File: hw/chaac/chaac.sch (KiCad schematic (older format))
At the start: 85 parts, among them J1 windrain, J10 Therm, J11 FAN, J2 Conn_01x02, J3 UART, J4 Battery, J5 Power, J6 Light, J7 AM2315, J8 TC2030-CTX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

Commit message: Began placement for chaac
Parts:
- removed L2: 47nH, Inductor_SMD:L_0603_1608Metric, symbol Device:L_Small
- removed R13, R14: 0, Resistor_SMD:R_0603_1608Metric, symbol Device:R_Small
- added C31: 0.1uF, Capacitor_SMD:C_0603_1608Metric, symbol Device:C_Small
- C11: value 22pF -> 0.1uF; DKPN 1276-2228-1-ND -> 490-1532-1-ND; MPN CL10C220JB8NFNC -> GRM188R71C104KA01D
- U7: footprint (none) -> alvarop:XCL102
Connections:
- net GPS_RXD is gone; now on net BATT: C11.1
- net GND: now also C31.2
- net LIGHT: now also C31.1
- net UART_TX: now also J3.3 (Pin_3)
- no-connect marks 24 -> 25
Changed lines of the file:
@@
 Text Label 2650 10900 1    50   ~ 0
 GPS_TXD
-Text Label 2750 10900 1    50   ~ 0
-GPS_RXD
 $Comp
 L power:+3.3V #PWR05
@@
 	8050 10450 8350 10450
 Wire Wire Line
-	8350 10450 8350 10550
+	8350 10450 8350 10650
 Wire Wire Line
 	8050 10550 8200 10550
@@
 L power:GND #PWR010
 U 1 1 5BAABEB2
-P 8350 10550
-F 0 "#PWR010" H 8350 10300 50  0001 C CNN
-F 1 "GND" H 8355 10377 50  0000 C CNN
-F 2 "" H 8350 10550 50  0001 C CNN
-F 3 "" H 8350 10550 50  0001 C CNN
-	1    8350 10550
-	1    0    0    -1
-$EndComp
-Wire Wire Line
-	8050 10350 8350 10350
-Text Label 8350 10350 2    50   ~ 0
+P 8350 10750
+F 0 "#PWR010" H 8350 10500 50  0001 C CNN
+F 1 "GND" H 8355 10577 50  0000 C CNN
+F 2 "" H 8350 10750 50  0001 C CNN
+F 3 "" H 8350 10750 50  0001 C CNN
+	1    8350 10750
+	1    0    0    -1
+$EndComp
+Wire Wire Line
+	8050 10350 8500 10350
+Text Label 8750 10350 2    50   ~ 0
 LIGHT
 $Comp
@@
 Text Label 8800 3000 2    50   ~ 0
 XB_TX
-Wire Wire Line
-	2200 1900 1850 1900
-Text Label 1850 1900 0    50   ~ 0
-GPS_RXD
 Wire Wire Line
 	8400 3300 8800 3300
@@
 	2000 10200 2150 10200
 $Comp
-L Device:L_Small L2
-U 1 1 5C41F42C
-P 2750 10300
-F 0 "L2" H 2798 10346 50  0000 L CNN
-F 1 "47nH" H 2798 10255 50  0000 L CNN
-F 2 "Inductor_SMD:L_0603_1608Metric" H 2750 10300 50  0001 C CNN
-F 3 "~" H 2750 10300 50  0001 C CNN
-F 4 " ‎L-14C47NJV4T" H 2750 10300 50  0001 C CNN "MPN"
-F 5 "712-1442-1-ND‎" H 2750 10300 50  0001 C CNN "DKPN"
-	1    2750 10300
-	1    0    0    -1
-$EndComp
-$Comp
 L Device:L_Small L1
 U 1 1 5C41F6C3
@@
 Wire Wire Line
 	2650 10200 2650 10150
-Wire Wire Line
-	2750 10150 2750 10200
 $Comp
 L power:GND #PWR0110
@@
 Wire Wire Line
 	2650 10400 2650 10500
-Wire Wire Line
-	2750 10400 2750 10500
 $Comp
 L Device:C_Small C8
@@
 	0    -1   -1   0
 $EndComp
-$Comp
-L Device:C_Small C11
-U 1 1 5C49A200
-P 2950 10500
-F 0 "C11" H 2750 10550 50  0000 L CNN
-F 1 "22pF" H 2700 10450 50  0000 L CNN
-F 2 "Capacitor_SMD:C_0603_1608Metric" H 2950 10500 50  0001 C CNN
-F 3 "~" H 2950 10500 50  0001 C CNN
-F 4 "1276-2228-1-ND" H 0   0   50  0001 C CNN "DKPN"
-F 5 "CL10C220JB8NFNC" H 0   0   50  0001 C CNN "MPN"
-	1    2950 10500
-	0    -1   -1   0
-$EndComp
-Wire Wire Line
-	2850 10500 2750 10500
-Connection ~ 2750 10500
-Wire Wire Line
-	2750 10500 2750 10900
 Wire Wire Line
 	2650 10500 2550 10500
@@
 Wire Wire Line
 	2300 10500 2350 10500
-$Comp
-L power:GND #PWR0115
-U 1 1 5C4BAD54
-P 3100 10500
-F 0 "#PWR0115" H 3100 10250 50  0001 C CNN
-F 1 "GND" H 3105 10327 50  0000 C CNN
-F 2 "" H 3100 10500 50  0001 C CNN
-F 3 "" H 3100 10500 50  0001 C CNN
-	1    3100 10500
-	0    -1   -1   0
-$EndComp
-Wire Wire Line
-	3050 10500 3100 10500
 Wire Wire Line
 	2050 9650 1650 9650
@@
 UART_RX
 $Comp
-L Device:R_Small R13
-U 1 1 5C9B2177
-P 2300 1750
-F 0 "R13" V 2350 1650 50  0000 C CNN
-F 1 "0" V 2300 1750 50  0000 C CNN
-F 2 "Resistor_SMD:R_0603_1608Metric" H 2300 1750 50  0001 C CNN
-F 3 "~" H 2300 1750 50  0001 C CNN
-	1    2300 1750
-	0    -1   -1   0
-$EndComp
-$Comp
-L Device:R_Small R14
-U 1 1 5C9C0DF4
-P 2300 1900
-F 0 "R14" V 2250 2000 50  0000 C CNN
-F 1 "0" V 2300 1900 50  0000 C CNN
-F 2 "Resistor_SMD:R_0603_1608Metric" H 2300 1900 50  0001 C CNN
-F 3 "~" H 2300 1900 50  0001 C CNN
-	1    2300 1900
-	0    1    1    0
-$EndComp
-Wire Wire Line
-	2400 1750 2450 1750
-Wire Wire Line
-	2050 1750 2200 1750
-Wire Wire Line
-	2400 1900 2450 1900
-Wire Wire Line
-	2450 1900 2450 1750
-Connection ~ 2450 1750
-Wire Wire Line
-	2450 1750 2800 1750
-$Comp
 L Device:R_Small R7
 U 1 1 5CAA119E
@@
 $EndComp
 Wire Wire Line
-	1000 1350 1000 1500
+	1000 1350 1000 1450
 Wire Wire Line
 	1000 850  1000 700
@@
 Wire Wire Line
 	1000 1100 1000 1150
-Text Label 1350 1100 2    50   ~ 0
+Text Label 1550 1100 2    50   ~ 0
 BATT
 $Comp
@@
 U 1 1 5CE242B1
 P 14350 7600
-F 0 "R22" V 14450 7750 50  0000 R CNN
+F 0 "R22" V 14550 7750 50  0000 R CNN
 F 1 "10k" V 14450 7650 50  0000 R CNN
 F 2 "Resistor_SMD:R_0603_1608Metric" H 14350 7600 50  0001 C CNN
@@
 U 1 1 5CE248E2
 P 14350 7900
-F 0 "R23" V 14450 8050 50  0000 R CNN
+F 0 "R23" V 14550 8050 50  0000 R CNN
 F 1 "10k" V 14450 7950 50  0000 R CNN
 F 2 "Resistor_SMD:R_0603_1608Metric" H 14350 7900 50  0001 C CNN
@@
 U 1 1 5CE2498A
 P 14350 8250
-F 0 "R24" V 14250 8350 50  0000 R CNN
+F 0 "R24" V 14200 8350 50  0000 R CNN
 F 1 "10k" V 14250 8200 50  0000 R CNN
 F 2 "Resistor_SMD:R_0603_1608Metric" H 14350 8250 50  0001 C CNN
@@
 P 11400 7800
 F 0 "R17" V 11500 7950 50  0000 R CNN
-F 1 "10k" V 11500 7850 50  0000 R CNN
+F 1 "10k" V 11500 7750 50  0000 R CNN
 F 2 "Resistor_SMD:R_0603_1608Metric" H 11400 7800 50  0001 C CNN
 F 3 "~" H 11400 7800 50  0001 C CNN
@@
 F 0 "U7" H 2250 4800 60  0000 C CNN
 F 1 "XCL102" H 2250 4694 60  0000 C CNN
-F 2 "" H 1800 4200 50  0001 C CNN
+F 2 "alvarop:XCL102" H 1800 4200 50  0001 C CNN
 F 3 "" H 1800 4200 50  0001 C CNN
 	1    2250 4100
@@
 Wire Wire Line
 	3500 4300 3550 4300
+Wire Wire Line
+	2050 1750 2800 1750
+NoConn ~ 2750 10150
+$Comp
+L Device:C_Small C11
+U 1 1 5DEB196A
+P 1350 1300
+F 0 "C11" H 1200 1450 50  0000 L CNN
+F 1 "0.1uF" H 1100 1200 50  0000 L CNN
+F 2 "Capacitor_SMD:C_0603_1608Metric" H 1350 1300 50  0001 C CNN
+F 3 "~" H 1350 1300 50  0001 C CNN
+F 4 "490-1532-1-ND" H -4900 -7050 50  0001 C CNN "DKPN"
+F 5 "GRM188R71C104KA01D" H -4900 -7050 50  0001 C CNN "MPN"
+	1    1350 1300
+	1    0    0    -1
+$EndComp
+Wire Wire Line
+	1350 1200 1350 1100
+Connection ~ 1350 1100
+Wire Wire Line
+	1350 1100 1550 1100
+Wire Wire Line
+	1350 1400 1350 1450
+Wire Wire Line
+	1350 1450 1000 1450
+Connection ~ 1000 1450
+Wire Wire Line
+	1000 1450 1000 1500
+$Comp
+L Device:C_Small C31
+U 1 1 5DF1B210
+P 8500 10500
+F 0 "C31" H 8600 10450 50  0000 L CNN
+F 1 "0.1uF" H 8550 10600 50  0000 L CNN
+F 2 "Capacitor_SMD:C_0603_1608Metric" H 8500 10500 50  0001 C CNN
+F 3 "~" H 8500 10500 50  0001 C CNN
+F 4 "490-1532-1-ND" H 2250 2150 50  0001 C CNN "DKPN"
+F 5 "GRM188R71C104KA01D" H 2250 2150 50  0001 C CNN "MPN"
+	1    8500 10500
+	1    0    0    -1
+$EndComp
+Wire Wire Line
+	8500 10400 8500 10350
+Connection ~ 8500 10350
+Wire Wire Line
+	8500 10350 8750 10350
+Wire Wire Line
+	8500 10600 8500 10650
+Wire Wire Line
+	8500 10650 8350 10650
+Connection ~ 8350 10650
+Wire Wire Line
+	8350 10650 8350 10750
 $EndSCHEMATC

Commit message: Removed GPS, re-did placement
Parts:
- removed ANT1: SR4G008, alvarop:SR4G008, symbol alvarop:SR4G008
- removed C13, C15, C6, C8: 22pF, Capacitor_SMD:C_0603_1608Metric, symbol Device:C_Small
- removed C7: 2.2uF, Capacitor_SMD:C_0603_1608Metric, symbol Device:C_Small
- removed C9: 1.5pF, Capacitor_SMD:C_0402_1005Metric, symbol Device:C_Small
- removed L1: 47nH, Inductor_SMD:L_0603_1608Metric, symbol Device:L_Small
- removed L3: 12nH, Inductor_SMD:L_0402_1005Metric, symbol Device:L_Small
- removed L4: DNP, Inductor_SMD:L_0402_1005Metric, symbol Device:L_Small
- removed U4: M10578-A2, alvarop:M10578-A2, symbol alvarop:M10578-A2
- added J12: AM2315, Connector_PinHeader_2.54mm:PinHeader_1x04_P2.54mm_Vertical, symbol Connector_Generic:Conn_01x04
- added R13: 0, Resistor_SMD:R_0603_1608Metric, symbol Device:R_Small
- R11: value 10k -> 0; DKPN 311-10.0KHRCT-ND -> (none); MPN RC0603FR-0710KL -> (none)
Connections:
- net +3V3: now also J12.2 (Pin_2)
- net GND: now also J12.1 (Pin_1); no longer R11.1
- net GPS_SBY: now also U2.31 (PH3/BOOT0), J12.4 (Pin_4); no longer U2.26 (PB3)
- net LED1: now also U2.21 (PA11); no longer U2.27 (PB4)
- net UART_RX: now also R11.1, R13.1; no longer J3.2 (Pin_2)
- net GPS_TX: now reaches R11.2
- net GPS_TX: now also J12.3 (Pin_3)
- net GPS_FIX: no longer names the net of U2.15 (PB1)
- net GPS_TXD: no longer names the net of U2.25 (PA15/SWO)
- new net: J3.2 (Pin_2), R13.2
- no-connect marks 25 -> 21
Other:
- moved on the sheet: C10, C12, C14, J1, R1, R15, R2, R3, R4, R5, R6

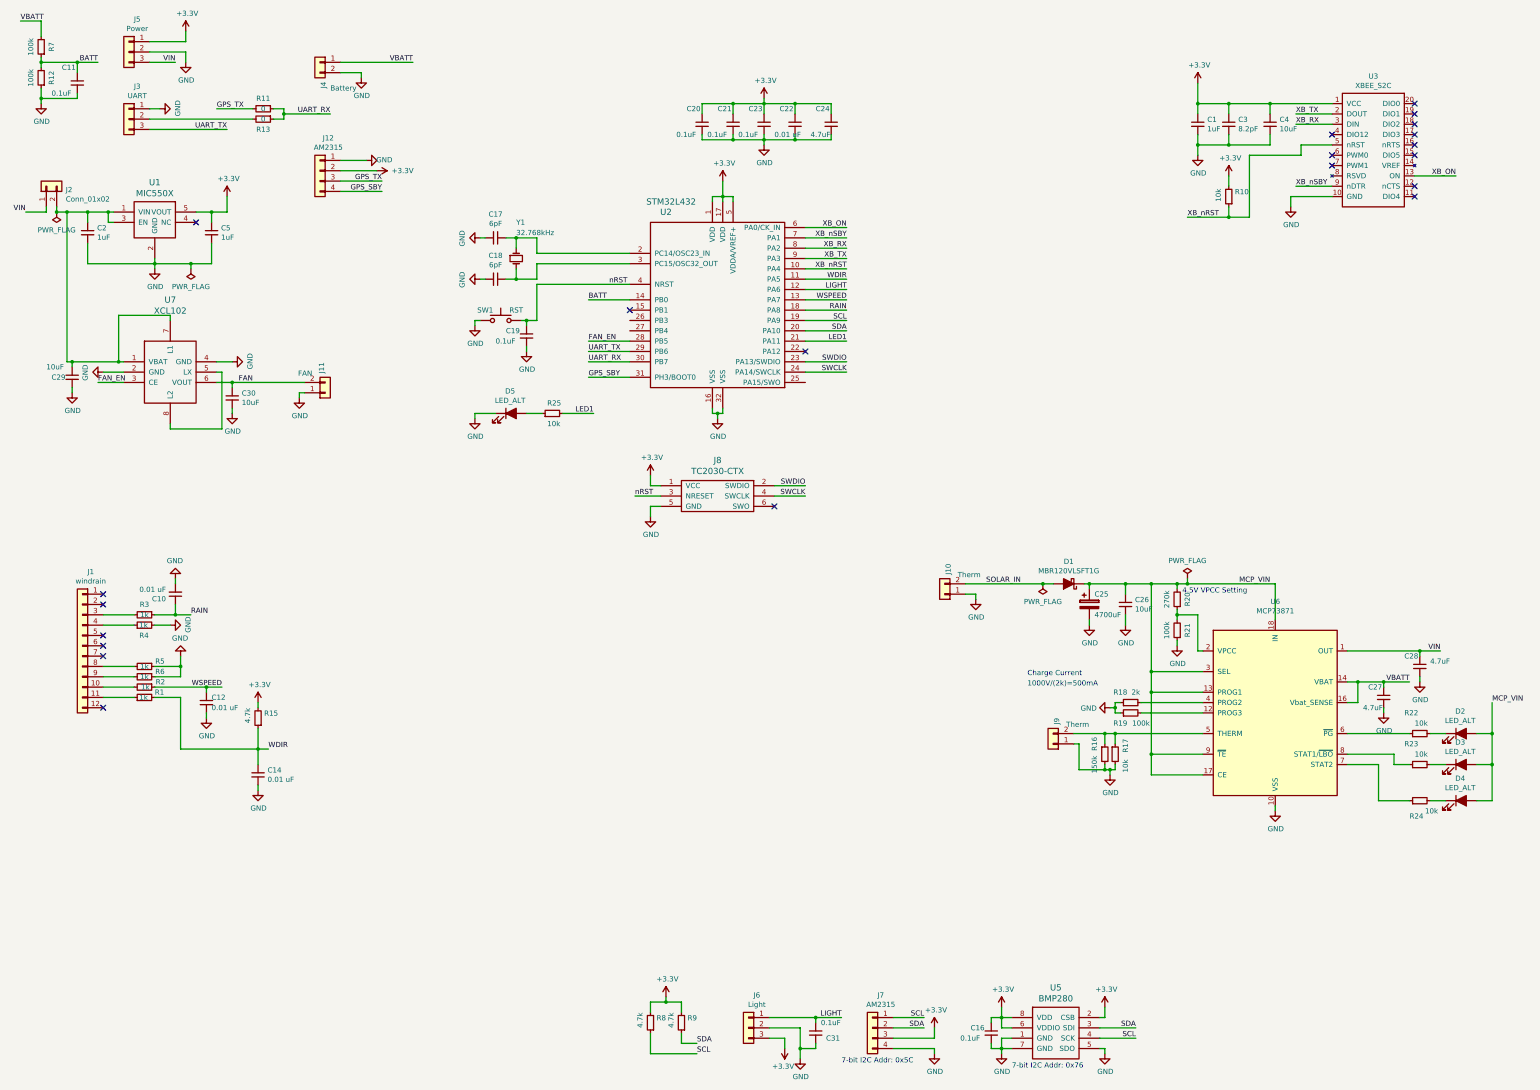
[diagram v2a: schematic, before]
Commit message: Finished chaac 1.0 schematic and layout
Released to JLCPCB
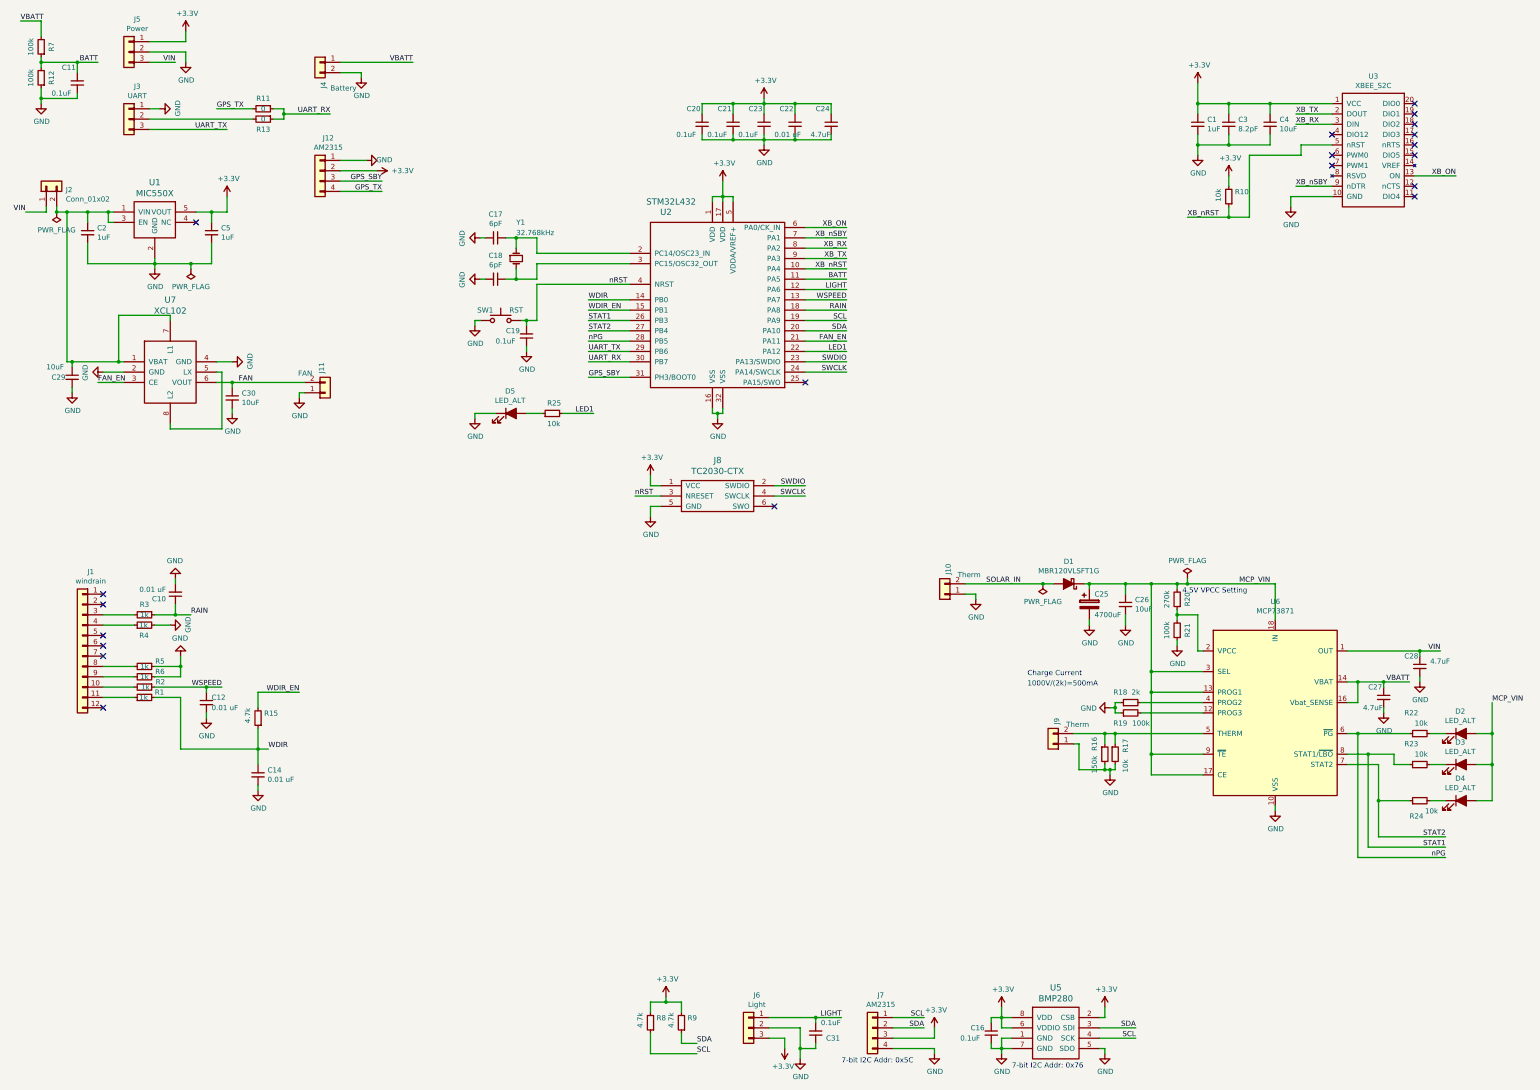
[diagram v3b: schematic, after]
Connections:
- net +3V3: no longer R15.2
- net BATT: now also U2.11 (PA5); no longer U2.14 (PB0)
- net FAN_EN: now also U2.21 (PA11); no longer U2.28 (PB5)
- net GPS_SBY: now also J12.3 (Pin_3); no longer J12.4 (Pin_4)
- net GPS_TX: now also J12.4 (Pin_4); no longer J12.3 (Pin_3)
- net LED1: now also U2.22 (PA12); no longer U2.21 (PA11)
- net WDIR: now also U2.14 (PB0); no longer U2.11 (PA5)
- net WDIR_EN: now reaches U2.15 (PB1)
- net WDIR_EN: now also R15.2
- net STAT1: now reaches U2.26 (PB3)
- net STAT1: now also R23.1, U6.8 (STAT1/~LBO~)
- net STAT2: now reaches U2.27 (PB4)
- net STAT2: now also R24.1, U6.7 (STAT2)
- net nPG: now reaches R22.1, U6.6 (~PG~)
- net nPG: now also U2.28 (PB5)
- no-connect marks 21 -> 20
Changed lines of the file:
@@
 Sheet 1 1
 Title "Chaac"
-Date "2019-01-02"
+Date "2019-01-03"
 Rev "1.0"
 Comp "@alvaroprieto"
@@
 Wire Wire Line
 	8400 3200 8800 3200
-Text Label 8800 3200 2    50   ~ 0
+Text Label 6300 3400 0    50   ~ 0
 WDIR
 Wire Wire Line
@@
 Wire Wire Line
 	3100 7550 3100 7750
-$Comp
-L power:+3.3V #PWR0123
-U 1 1 5C2B14C9
-P 3100 7300
-F 0 "#PWR0123" H 3100 7150 50  0001 C CNN
-F 1 "+3.3V" H 3115 7473 50  0000 C CNN
-F 2 "" H 3100 7300 50  0001 C CNN
-F 3 "" H 3100 7300 50  0001 C CNN
-	1    3100 7300
-	1    0    0    -1
-$EndComp
-Wire Wire Line
-	3100 7300 3100 7350
 Text Label 3200 7750 0    50   ~ 0
 WDIR
@@
 Text Label 6300 4000 0    50   ~ 0
 UART_RX
-Text Label 6300 3400 0    50   ~ 0
+Text Label 8800 3200 2    50   ~ 0
 BATT
 Wire Wire Line
@@
 $EndComp
 Wire Wire Line
-	14250 7600 13650 7600
-Wire Wire Line
-	13650 7800 14100 7800
+	14250 7600 13750 7600
+Wire Wire Line
+	13650 7800 13850 7800
 Wire Wire Line
 	14100 7800 14100 7900
@@
 	1    0    0    -1
 $EndComp
-NoConn ~ 8400 3900
 $Comp
 L power:PWR_FLAG #FLG0106
@@
 Wire Wire Line
 	12100 6150 12950 6150
-Text Label 8800 3800 2    50   ~ 0
+Text Label 8800 3900 2    50   ~ 0
 LED1
 $Comp
@@
 	5200 4500 5200 4550
 Wire Wire Line
-	6700 3800 6300 3800
-Text Label 6300 3800 0    50   ~ 0
+	8400 3800 8800 3800
+Text Label 8800 3800 2    50   ~ 0
 FAN_EN
 $Comp
@@
 	0    1    1    0
 $EndComp
+Text Label 4300 2250 2    50   ~ 0
+GPS_SBY
 Text Label 4300 2350 2    50   ~ 0
-GPS_SBY
-Text Label 4300 2250 2    50   ~ 0
 GPS_TX
 Wire Wire Line
-	8400 3800 8800 3800
-NoConn ~ 6700 3500
+	8400 3900 8800 3900
+Wire Wire Line
+	6700 3500 6300 3500
+Text Label 6300 3500 0    50   ~ 0
+WDIR_EN
+Text Label 3500 7200 2    50   ~ 0
+WDIR_EN
+Wire Wire Line
+	3100 7200 3500 7200
+Wire Wire Line
+	3100 7200 3100 7350
+Wire Wire Line
+	13950 8250 13950 8600
+Wire Wire Line
+	13950 8600 14600 8600
+Connection ~ 13950 8250
+Wire Wire Line
+	13850 7800 13850 8700
+Wire Wire Line
+	13850 8700 14600 8700
+Connection ~ 13850 7800
+Wire Wire Line
+	13850 7800 14100 7800
+Wire Wire Line
+	13750 7600 13750 8800
+Wire Wire Line
+	13750 8800 14600 8800
+Connection ~ 13750 7600
+Wire Wire Line
+	13750 7600 13650 7600
+Text Label 14600 8700 2    50   ~ 0
+STAT1
+Text Label 14600 8600 2    50   ~ 0
+STAT2
+Text Label 14600 8800 2    50   ~ 0
+nPG
+Wire Wire Line
+	6700 3600 6300 3600
+Wire Wire Line
+	6700 3700 6300 3700
+Wire Wire Line
+	6700 3800 6300 3800
+Text Label 6300 3600 0    50   ~ 0
+STAT1
+Text Label 6300 3700 0    50   ~ 0
+STAT2
+Text Label 6300 3800 0    50   ~ 0
+nPG
+NoConn ~ 8400 4200
 $EndSCHEMATC
